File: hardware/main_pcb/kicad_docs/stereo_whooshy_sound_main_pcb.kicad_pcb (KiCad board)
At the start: 2 copper layers, 134.6 x 58.4 mm, 33 parts, among them J1 signal_in_A, J10 audio_in_B, J11 audio_out_A, J12 audio_out_B, J13 9vdc_in, J14 CV_in_B, J15 CV_in_A, J2 freq_CV_in_A, J3 signal_out_A, J4 feedback_CV_and_PS_A, J5 signal_in_B, J6 freq_CV_in_B, J7 signal_out_B, J8 feedback_CV_and_PS_B, J9 audio_in_A, U1 TL072, U2 CD74HC4067SM, U3 STM32G071KxT, U4 TL072, U5 MCP6002-xSN, U6 MCP6002-xSN, U7 MCP6002-xSN

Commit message: progress on schemo
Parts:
- removed the J11 at (81.3, 2.54)
- removed the J12 at (19.1, 2.54)
- removed the U4 at (180.0, 43.5)
- added U2: TL072, Package_SO:SOIC-8_3.9x4.9mm_P1.27mm, B.Cu at (143.5, 26.7)
- added U8: TLV1117-33, Package_TO_SOT_SMD:SOT-223-3_TabPin2, B.Cu at (158.8, 45.7)
- J10: value audio_in_B -> IO_B; footprint Connector_PinHeader_2.54mm:PinHeader_1x02_P2.54mm_Vertical -> Connector_PinHeader_2.54mm:PinHeader_1x03_P2.54mm_Vertical
- J9: value audio_in_A -> IO_A; footprint Connector_PinHeader_2.54mm:PinHeader_1x02_P2.54mm_Vertical -> Connector_PinHeader_2.54mm:PinHeader_1x03_P2.54mm_Vertical
- U1: moved to B.Cu
- U3: renamed from U5; moved to B.Cu
- U4: renamed from U6; moved to B.Cu
- U5: renamed from U7; moved to B.Cu
- U6: renamed from U2; moved to B.Cu
- U7: renamed from U3; moved to B.Cu
- moved J12 63.2 mm to (21.6, 2.54)
- moved J11 55.1 mm to (77.5, 2.54)
- moved U5 42.8 mm to (140.0, 37.9), turned to 180 degrees
- moved U3 36.3 mm to (176.5, 30.5), turned to 180 degrees
- moved U7 33.6 mm to (175.0, 17.4), turned to 180 degrees
- moved U6 25.0 mm to (150.1, 16.7), turned to 180 degrees
- moved U4 22.1 mm to (168.0, 30.5), turned to 180 degrees
- moved U1 18.3 mm to (154.9, 30.5), turned to 180 degrees
- moved J9 5.08 mm to (102.9, 2.54)
- moved J10 1.27 mm to (47.0, 2.54)
- renumbered J15 to J11, J14 to J12
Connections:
- net Net-(J10-Pad1) renamed /audio_in_B
- net Net-(J9-Pad1) renamed /audio_in_A
- J10 pad 2: GND -> /audio_out_B
- J9 pad 2: GND -> /audio_out_A
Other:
- board size 134.6 x 58.4 mm -> 134.6 x 82.6 mm

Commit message: progress on pcb layout
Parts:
- added C1: 4n7, Capacitor_SMD:C_0805_2012Metric, B.Cu at (128.9, 29.1)
- added C10: 100n, Capacitor_SMD:C_0603_1608Metric, B.Cu at (90.6, 97.8)
- added C11: 10u, Capacitor_SMD:C_0805_2012Metric, B.Cu at (45.1, 17.7)
- added C12: 100n, Capacitor_SMD:C_0603_1608Metric, B.Cu at (93.6, 97.8)
- added C13: 10u, Capacitor_SMD:C_0805_2012Metric, B.Cu at (45.1, 23.0)
- added C14: 1u, Capacitor_SMD:C_0805_2012Metric, B.Cu at (74.8, 100.0)
- added C15: 100n, Capacitor_SMD:C_0603_1608Metric, B.Cu at (78.5, 100.3)
- added C16: 4u7, Capacitor_SMD:C_0805_2012Metric, B.Cu at (51.4, 111.4)
- added C17: 100n, Capacitor_SMD:C_0603_1608Metric, B.Cu at (56.4, 111.5)
- added C18: 100n, Capacitor_SMD:C_0603_1608Metric, B.Cu at (14.7, 69.2)
- added C19: 1u, Capacitor_SMD:C_0805_2012Metric, B.Cu at (47.2, 100.4)
- added C2: 4n7, Capacitor_SMD:C_0805_2012Metric, B.Cu at (91.4, 29.3)
- added C20: 100n, Capacitor_SMD:C_0603_1608Metric, B.Cu at (14.8, 72.4)
- added C21: 1u, Capacitor_SMD:C_0805_2012Metric, B.Cu at (51.1, 100.4)
- added C22: 4u7, Capacitor_SMD:C_0805_2012Metric, B.Cu at (61.2, 90.7)
- added C23: 100n, Capacitor_SMD:C_0603_1608Metric, B.Cu at (90.8, 59.5)
- added C24: 4u7, Capacitor_SMD:C_0805_2012Metric, B.Cu at (61.2, 94.8)
- added C25: 10u bp, Capacitor_THT:C_Radial_D6.3mm_H11.0mm_P2.50mm, B.Cu at (116.2, 29.2)
- added C26: 10u bp, Capacitor_THT:C_Radial_D6.3mm_H11.0mm_P2.50mm, B.Cu at (78.7, 29.2)
- added C28: 22n, Capacitor_SMD:C_0603_1608Metric, B.Cu at (84.5, 54.8)
- added C3: 10u, Capacitor_SMD:C_0805_2012Metric, B.Cu at (95.4, 106.4)
- added C31: 100n, Capacitor_SMD:C_0603_1608Metric, B.Cu at (58.9, 59.1)
- added C33: 22n, Capacitor_SMD:C_0603_1608Metric, B.Cu at (49.5, 54.0)
- added C34: 22n, Capacitor_SMD:C_0603_1608Metric, B.Cu at (49.5, 68.2)
- added C35: 100n, Capacitor_SMD:C_0603_1608Metric, B.Cu at (82.0, 92.7)
- added C36: 100n, Capacitor_SMD:C_0603_1608Metric, B.Cu at (85.3, 92.7)
- added C37: 100n, Capacitor_SMD:C_0603_1608Metric, B.Cu at (88.6, 92.7)
- added C38: 100n, Capacitor_SMD:C_0603_1608Metric, B.Cu at (91.7, 92.7)
- added C39: 100n, Capacitor_SMD:C_0603_1608Metric, B.Cu at (94.7, 92.7)
- added C4: 100n, Capacitor_SMD:C_0603_1608Metric, B.Cu at (106.8, 28.4)
- added C40: 100n, Capacitor_SMD:C_0603_1608Metric, B.Cu at (86.5, 108.7)
- added C41: 100n, Capacitor_SMD:C_0603_1608Metric, B.Cu at (78.7, 92.7)
- added C42: 1u, Capacitor_SMD:C_0805_2012Metric, B.Cu at (79.6, 108.9)
- added C43: 1u, Capacitor_SMD:C_0805_2012Metric, B.Cu at (83.2, 108.9)
- added C44: 470n, Capacitor_SMD:C_0805_2012Metric, B.Cu at (34.2, 54.9)
- added C45: 470n, Capacitor_SMD:C_0805_2012Metric, B.Cu at (34.2, 80.7)
- added C46: 100n, Capacitor_SMD:C_0603_1608Metric, B.Cu at (48.9, 62.4)
- added C47: 100n, Capacitor_SMD:C_0603_1608Metric, B.Cu at (92.8, 66.1)
- added C48: 100n, Capacitor_SMD:C_0603_1608Metric, B.Cu at (113.2, 70.9)
- added C49: 100n, Capacitor_SMD:C_0603_1608Metric, B.Cu at (113.2, 74.9)
- added C5: 100n, Capacitor_SMD:C_0603_1608Metric, B.Cu at (106.8, 32.5)
- added C50: 100n, Capacitor_SMD:C_0603_1608Metric, B.Cu at (103.8, 70.9)
- added C51: 100n, Capacitor_SMD:C_0603_1608Metric, B.Cu at (103.8, 74.9)
- added C52: 100n, Capacitor_SMD:C_0603_1608Metric, B.Cu at (90.4, 38.8)
- added C53: 100n, Capacitor_SMD:C_0603_1608Metric, B.Cu at (90.4, 42.9)
- added C54: 100n, Capacitor_SMD:C_0603_1608Metric, B.Cu at (115.7, 39.0)
- added C55: 100n, Capacitor_SMD:C_0603_1608Metric, B.Cu at (115.7, 43.1)
- added C6: 100n, Capacitor_SMD:C_0603_1608Metric, B.Cu at (95.4, 111.8)
- added C7: 100n, Capacitor_SMD:C_0603_1608Metric, B.Cu at (34.7, 47.9)
- added C8: 100n, Capacitor_SMD:C_0603_1608Metric, B.Cu at (35.2, 73.9)
- added C9: 10u, Capacitor_SMD:C_0805_2012Metric, B.Cu at (96.9, 97.7)
- added D1: B5819W, Diode_SMD:D_SOD-123, B.Cu at (60.3, 15.9)
- added D2: PMEG2010AEH, Diode_SMD:D_SOD-123F, B.Cu at (51.9, 96.3)
- added D3: PMEG2010AEH, Diode_SMD:D_SOD-123F, B.Cu at (59.1, 101.9)
- added D4: PMEG2010AEH, Diode_SMD:D_SOD-123F, B.Cu at (59.1, 98.3)
- added D5: PMEG2010AEH, Diode_SMD:D_SOD-123F, B.Cu at (51.9, 92.7)
- added D6: LED, LED_THT:LED_D5.0mm, F.Cu at (33.7, 104.1)
- added D7: LED, LED_THT:LED_D5.0mm, F.Cu at (107.3, 104.1)
- added FB1: 100R @ 100MHz, Inductor_SMD:L_0805_2012Metric, B.Cu at (49.6, 16.5)
- added FB2: 100R @ 100MHz, Inductor_SMD:L_0805_2012Metric, B.Cu at (71.9, 92.9)
- added FB3: 100R @ 100MHz, Inductor_SMD:L_0805_2012Metric, B.Cu at (47.0, 111.6)
- added FB4: 100R @ 100MHz, Inductor_SMD:L_0805_2012Metric, B.Cu at (19.7, 70.9)
- added J14: feedback_CV_and_PS_B, Connector_PinSocket_2.54mm:PinSocket_1x08_P2.54mm_Vertical, B.Cu at (6.99, 66.0)
- added J15: swd_header, Connector_PinHeader_2.54mm:PinHeader_1x04_P2.54mm_Vertical, B.Cu at (67.3, 110.5)
- added J16: Jack-DC, Connector_BarrelJack:BarrelJack_CUI_PJ-063AH_Horizontal, B.Cu at (52.7, 12.2)
- added J17: footswitch_A, Connector_PinHeader_2.54mm:PinHeader_1x02_P2.54mm_Vertical, B.Cu at (33.7, 108.0)
- added J18: footswitch_B, Connector_PinHeader_2.54mm:PinHeader_1x02_P2.54mm_Vertical, B.Cu at (107.3, 108.0)
- added L1: 10uH, 1.2A, Inductor_SMD:L_Taiyo-Yuden_NR-50xx, B.Cu at (50.0, 105.7)
- added R1: 2M2, Resistor_SMD:R_0603_1608Metric, B.Cu at (132.7, 29.0)
- added R10: 13k3, Resistor_SMD:R_0603_1608Metric, B.Cu at (63.8, 105.9)
- added R11: 20k, Resistor_SMD:R_0603_1608Metric, B.Cu at (87.6, 59.5)
- added R12: 1k2, Resistor_SMD:R_0603_1608Metric, B.Cu at (111.1, 33.2)
- added R13: 1k2, Resistor_SMD:R_0603_1608Metric, B.Cu at (87.0, 33.6)
- added R14: 10k, Resistor_SMD:R_0603_1608Metric, B.Cu at (120.9, 29.1)
- added R15: 10k, Resistor_SMD:R_0603_1608Metric, B.Cu at (73.0, 27.8)
- added R16: R, Resistor_SMD:R_0603_1608Metric, B.Cu at (39.2, 101.9)
- added R17: R, Resistor_SMD:R_0603_1608Metric, B.Cu at (104.6, 102.3)
- added R18: 1M, Resistor_SMD:R_0603_1608Metric, B.Cu at (89.5, 72.8)
- added R19: 1M, Resistor_SMD:R_0603_1608Metric, B.Cu at (86.4, 72.8)
- added R2: 2M2, Resistor_SMD:R_0603_1608Metric, B.Cu at (125.1, 29.0)
- added R20: 300k, Resistor_SMD:R_0603_1608Metric, B.Cu at (90.8, 54.8)
- added R21: 120k, Resistor_SMD:R_0603_1608Metric, B.Cu at (87.6, 54.8)
- added R22: 10k, Resistor_SMD:R_0603_1608Metric, B.Cu at (26.8, 37.1)
- added R23: 10k, Resistor_SMD:R_0603_1608Metric, B.Cu at (15.4, 37.7)
- added R24: 100k, Resistor_SMD:R_0603_1608Metric, B.Cu at (58.9, 68.3)
- added R25: 300k, Resistor_SMD:R_0603_1608Metric, B.Cu at (62.0, 63.8)
- added R26: 120k, Resistor_SMD:R_0603_1608Metric, B.Cu at (62.0, 59.0)
- added R27: 12k, Resistor_SMD:R_0603_1608Metric, B.Cu at (62.0, 68.3)
- added R28: 10k, Resistor_SMD:R_0603_1608Metric, B.Cu at (62.2, 53.9)
- added R29: 300k, Resistor_SMD:R_0603_1608Metric, B.Cu at (49.5, 49.5)
- added R3: 2M2, Resistor_SMD:R_0603_1608Metric, B.Cu at (95.9, 29.4)
- added R30: 120k, Resistor_SMD:R_0603_1608Metric, B.Cu at (52.6, 49.5)
- added R31: 120k, Resistor_SMD:R_0603_1608Metric, B.Cu at (55.9, 49.6)
- added R32: 120k, Resistor_SMD:R_0603_1608Metric, B.Cu at (58.9, 49.5)
- added R33: 300k, Resistor_SMD:R_0603_1608Metric, B.Cu at (55.9, 53.9)
- added R34: 100k, Resistor_SMD:R_0603_1608Metric, B.Cu at (58.9, 53.9)
- added R35: 300k, Resistor_SMD:R_0603_1608Metric, B.Cu at (49.5, 72.7)
- added R36: 300k, Resistor_SMD:R_0603_1608Metric, B.Cu at (52.6, 72.7)
- added R37: 120k, Resistor_SMD:R_0603_1608Metric, B.Cu at (58.9, 72.7)
- added R38: 120k, Resistor_SMD:R_0603_1608Metric, B.Cu at (62.0, 72.7)
- added R4: 2M2, Resistor_SMD:R_0603_1608Metric, B.Cu at (87.0, 29.5)
- added R40: 120k, Resistor_SMD:R_0603_1608Metric, B.Cu at (52.6, 53.9)
- added R41: 120k, Resistor_SMD:R_0603_1608Metric, B.Cu at (52.6, 68.3)
- added R42: 10k, Resistor_SMD:R_0603_1608Metric, B.Cu at (75.4, 92.6)
- added R43: 20k, Resistor_SMD:R_0603_1608Metric, B.Cu at (26.8, 40.9)
- added R44: 10k, Resistor_SMD:R_0603_1608Metric, B.Cu at (29.8, 40.9)
- added R45: 30k, Resistor_SMD:R_0603_1608Metric, B.Cu at (23.7, 40.8)
- added R46: 4k7, Resistor_SMD:R_0603_1608Metric, B.Cu at (35.9, 40.9)
- added R47: 1k2, Resistor_SMD:R_0603_1608Metric, B.Cu at (32.9, 40.9)
- added R48: 100k, Resistor_SMD:R_0603_1608Metric, B.Cu at (27.8, 54.9)
- added R49: 100k, Resistor_SMD:R_0603_1608Metric, B.Cu at (30.9, 54.9)
- added R5: 2k2, Resistor_SMD:R_0603_1608Metric, B.Cu at (19.7, 75.7)
- added R50: 100k, Resistor_SMD:R_0603_1608Metric, B.Cu at (24.8, 54.9)
- added R51: 10k, Resistor_SMD:R_0603_1608Metric, B.Cu at (42.8, 101.9)
- added R52: 10k, Resistor_SMD:R_0603_1608Metric, B.Cu at (101.2, 102.3)
- added R53: 1M, Resistor_SMD:R_0603_1608Metric, B.Cu at (42.8, 105.6)
- added R54: 1M, Resistor_SMD:R_0603_1608Metric, B.Cu at (101.2, 106.2)
- added R55: 300k, Resistor_SMD:R_0603_1608Metric, B.Cu at (58.9, 63.8)
- added R57: 20k, Resistor_SMD:R_0603_1608Metric, B.Cu at (29.8, 67.1)
- added R58: 10k, Resistor_SMD:R_0603_1608Metric, B.Cu at (26.8, 67.1)
- added R59: 30k, Resistor_SMD:R_0603_1608Metric, B.Cu at (23.7, 67.1)
- added R6: 1R, Resistor_SMD:R_0603_1608Metric, B.Cu at (47.2, 95.6)
- added R60: 4k7, Resistor_SMD:R_0603_1608Metric, B.Cu at (35.9, 67.1)
- added R61: 1k2, Resistor_SMD:R_0603_1608Metric, B.Cu at (32.9, 67.1)
- added R62: 100k, Resistor_SMD:R_0603_1608Metric, B.Cu at (27.8, 80.6)
- added R63: 100k, Resistor_SMD:R_0603_1608Metric, B.Cu at (30.9, 80.6)
- added R64: 100k, Resistor_SMD:R_0603_1608Metric, B.Cu at (24.8, 80.6)
- added R65: 300k, Resistor_SMD:R_0603_1608Metric, B.Cu at (55.9, 72.7)
- added R66: 300k, Resistor_SMD:R_0603_1608Metric, B.Cu at (55.9, 68.3)
- added R7: 1R, Resistor_SMD:R_0603_1608Metric, B.Cu at (54.4, 100.5)
- added R8: 100k, Resistor_SMD:R_0603_1608Metric, B.Cu at (84.5, 59.5)
- added R9: 114k, Resistor_SMD:R_0603_1608Metric, B.Cu at (60.7, 105.9)
- added RV12: 100k trim, custom_footprints:bourns_3306F, B.Cu at (22.2, 30.5)
- added RV13: 100k trim, custom_footprints:bourns_3306F, B.Cu at (6.99, 30.5)
- added RV14: 100k trim, custom_footprints:bourns_3306F, B.Cu at (52.8, 30.5)
- added RV15: 100k trim, custom_footprints:bourns_3306F, B.Cu at (37.5, 30.5)
- added SW1: SW_DP_on_on_on, custom_footprints:DPDT_mini_toggle, F.Cu at (71.8, 36.8)
- added SW2: SW_SPDT_center_off, custom_footprints:SPDT_mini_toggle, F.Cu at (71.8, 58.4)
- added SW3: SW_SPDT, custom_footprints:SPDT_mini_toggle, F.Cu at (71.8, 80.0)
- added SW4: SW_DPDT_center_off, custom_footprints:DPDT_mini_toggle, F.Cu at (43.8, 80.0)
- added U10: STM32L031F4Px, Package_SO:TSSOP-20_4.4x6.5mm_P0.65mm, B.Cu at (84.6, 100.1)
- added U11: MCP4822, Package_SO:TSSOP-8_3x3mm_P0.65mm, B.Cu at (91.2, 108.7)
- added U12: LT1117-3.3, Package_TO_SOT_SMD:SOT-223-3_TabPin2, B.Cu at (52.2, 21.3)
- added U13: LT3467A, Package_TO_SOT_SMD:TSOT-23-6, B.Cu at (56.4, 107.2)
- added U14: LM4040DBZ-5, Package_TO_SOT_SMD:SOT-23, B.Cu at (14.9, 76.1)
- added U9: DG469EQ, Package_SO:MSOP-8_3x3mm_P0.65mm, B.Cu at (110.9, 40.9)
- J1: value signal_in_A -> NRJ6HM-1; footprint Connector_PinSocket_2.54mm:PinSocket_1x04_P2.54mm_Vertical -> Connector_Audio:Jack_6.35mm_Neutrik_NRJ6HM-1_Horizontal
- J10: value IO_B -> feedback_CV_and_PS_A; footprint Connector_PinHeader_2.54mm:PinHeader_1x03_P2.54mm_Vertical -> Connector_PinSocket_2.54mm:PinSocket_1x08_P2.54mm_Vertical
- J11: value CV_in_A -> signal_in_B; footprint Connector_PinHeader_2.54mm:PinHeader_1x03_P2.54mm_Vertical -> Connector_PinSocket_2.54mm:PinSocket_1x04_P2.54mm_Vertical
- J12: value CV_in_B -> signal_out_B; footprint Connector_PinHeader_2.54mm:PinHeader_1x03_P2.54mm_Vertical -> Connector_PinSocket_2.54mm:PinSocket_1x04_P2.54mm_Vertical
- J13: value 9vdc_in -> freq_CV_in_B; footprint Connector_PinHeader_2.54mm:PinHeader_1x02_P2.54mm_Vertical -> Connector_PinSocket_2.54mm:PinSocket_1x04_P2.54mm_Vertical
- J2: value freq_CV_in_A -> NRJ6HM-1; footprint Connector_PinSocket_2.54mm:PinSocket_1x04_P2.54mm_Vertical -> Connector_Audio:Jack_6.35mm_Neutrik_NRJ6HM-1_Horizontal
- J3: value signal_out_A -> NRJ6HM-1; footprint Connector_PinSocket_2.54mm:PinSocket_1x04_P2.54mm_Vertical -> Connector_Audio:Jack_6.35mm_Neutrik_NRJ6HM-1_Horizontal
- J4: value feedback_CV_and_PS_A -> NRJ6HM-1; footprint Connector_PinSocket_2.54mm:PinSocket_1x08_P2.54mm_Vertical -> Connector_Audio:Jack_6.35mm_Neutrik_NRJ6HM-1_Horizontal
- J5: value signal_in_B -> NRJ6HM-1; footprint Connector_PinSocket_2.54mm:PinSocket_1x04_P2.54mm_Vertical -> Connector_Audio:Jack_6.35mm_Neutrik_NRJ6HM-1_Horizontal
- J6: value freq_CV_in_B -> NRJ6HM-1; footprint Connector_PinSocket_2.54mm:PinSocket_1x04_P2.54mm_Vertical -> Connector_Audio:Jack_6.35mm_Neutrik_NRJ6HM-1_Horizontal
- J7: value signal_out_B -> signal_in_A
- J8: value feedback_CV_and_PS_B -> signal_out_A; footprint Connector_PinSocket_2.54mm:PinSocket_1x08_P2.54mm_Vertical -> Connector_PinSocket_2.54mm:PinSocket_1x04_P2.54mm_Vertical
- J9: value IO_A -> freq_CV_in_A; footprint Connector_PinHeader_2.54mm:PinHeader_1x03_P2.54mm_Vertical -> Connector_PinSocket_2.54mm:PinSocket_1x04_P2.54mm_Vertical
- RV4: value 10k -> 500k_dual; footprint Potentiometer_THT:Potentiometer_Alpha_RD901F-40-00D_Single_Vertical -> Potentiometer_THT:Potentiometer_Alpha_RD902F-40-00D_Dual_Vertical
- RV5: value 10k -> 10k_dual; footprint Potentiometer_THT:Potentiometer_Alpha_RD901F-40-00D_Single_Vertical -> Potentiometer_THT:Potentiometer_Alpha_RD902F-40-00D_Dual_Vertical
- U1: value TL072 -> TL074; footprint Package_SO:SOIC-8_3.9x4.9mm_P1.27mm -> Package_SO:TSSOP-14_4.4x5mm_P0.65mm
- U2: value TL072 -> MCP6004; footprint Package_SO:SOIC-8_3.9x4.9mm_P1.27mm -> Package_SO:TSSOP-14_4.4x5mm_P0.65mm
- U3, U4, U5: value MCP6002-xSN -> MCP6004; footprint Package_SO:SOIC-8_3.9x4.9mm_P1.27mm -> Package_SO:TSSOP-14_4.4x5mm_P0.65mm
- U6: value CD74HC4067SM -> DG469EQ; footprint Package_SO:SSOP-24_5.3x8.2mm_P0.65mm -> Package_SO:MSOP-8_3x3mm_P0.65mm
- U7: value STM32G071KxT -> DG469EQ; footprint Package_QFP:LQFP-32_7x7mm_P0.8mm -> Package_SO:MSOP-8_3x3mm_P0.65mm
- U8: value TLV1117-33 -> DG469EQ; footprint Package_TO_SOT_SMD:SOT-223-3_TabPin2 -> Package_SO:MSOP-8_3x3mm_P0.65mm
- moved U3 152.9 mm to (29.8, 73.9), turned to 270 degrees
- moved J7 136.5 mm to (134.0, 38.1)
- moved RV11 119.2 mm to (122.6, 87.6)
- moved U4 118.1 mm to (54.0, 61.1), turned to 270 degrees
- moved U2 116.0 mm to (29.5, 47.9), turned to 270 degrees
- moved J13 103.4 mm to (60.3, 76.2)
- moved U7 94.0 mm to (99.2, 72.9), turned to 270 degrees
- moved RV5 92.5 mm to (41.3, 66.1)
- moved RV3 90.2 mm to (13.4, 87.6)
- moved RV6 88.8 mm to (95.9, 44.5)
- moved J9 80.0 mm to (134.0, 76.2), turned to 180 degrees
- moved J8 79.5 mm to (80.6, 38.1)
- moved U8 72.9 mm to (86.0, 40.9), turned to 270 degrees
- moved J10 71.9 mm to (80.6, 66.0), turned to 180 degrees
- moved U6 70.0 mm to (108.3, 72.9), turned to 270 degrees
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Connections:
- J10 pad 1: /audio_in_B -> GND
- J10 pad 2: /audio_out_B -> GND
- J10 pad 3: Net-(J10-Pad3) -> /VCF_plug_in_board_ports/feedback_CV_in_A
- J11 pad 1: Net-(J11-Pad1) -> GND
- J11 pad 2: Net-(J11-Pad2) -> GND
- J11 pad 3: Net-(J11-Pad3) -> /switched_dry_B
- J12 pad 1: Net-(J12-Pad1) -> GND
- J12 pad 2: Net-(J12-Pad2) -> GND
- J12 pad 3: Net-(J12-Pad3) -> /bypass_switches/wet_in_B
- J13 pad 1: Net-(J13-Pad1) -> GND
- J13 pad 2: Net-(J13-Pad2) -> GND
- J7 pad 1: Net-(J7-Pad1) -> GND
- J7 pad 2: Net-(J7-Pad2) -> GND
- J7 pad 3: Net-(J7-Pad3) -> /dry_A
- J7 pad 4: Net-(J7-Pad4) -> /dry_A
- J8 pad 1: Net-(J8-Pad1) -> GND
- J8 pad 2: Net-(J8-Pad2) -> GND
- J8 pad 3: Net-(J8-Pad3) -> /wet_A
- J8 pad 4: Net-(J8-Pad4) -> /wet_A
- J9 pad 1: /audio_in_A -> GND
- J9 pad 2: /audio_out_A -> GND
- J9 pad 3: Net-(J9-Pad3) -> /VCF_plug_in_board_ports/freq_CV_in_A
- RV1 pad 2: /control_voltage_generators/scanned_potentiometers/initial_freq -> /control_voltage_generators/cv_summers/manual_freq
- RV1 pad 3: +3.3VA -> -5V
- RV10 pad 2: /control_voltage_generators/scanned_potentiometers/depth_B -> /control_voltage_generators/lfo/lfo_2_shape_cv
- RV11 pad 2: /control_voltage_generators/scanned_potentiometers/feedback -> /control_voltage_generators/lfo/lfo_2_depth_cv
- RV2 pad 2: /control_voltage_generators/scanned_potentiometers/env_lev_A -> /control_voltage_generators/cv_summers/separation_B
- RV2 pad 3: +3.3VA -> -5V
- RV3 pad 2: /control_voltage_generators/scanned_potentiometers/rate_A -> Net-(R20-Pad2)
- RV3 pad 3: +3.3VA -> -5V
- RV4 pad 1: GND -> Net-(R46-Pad1)
- RV4 pad 2: /control_voltage_generators/scanned_potentiometers/shape_A -> Net-(C44-Pad1)
- RV4 pad 3: +3.3VA -> Net-(C44-Pad1)
- RV5 pad 1: GND -> +1V0
- RV5 pad 2: /control_voltage_generators/scanned_potentiometers/depth_A -> /control_voltage_generators/cv_summers/env_A
- RV5 pad 3: +3.3VA -> Net-(R50-Pad1)
- RV6 pad 2: /control_voltage_generators/scanned_potentiometers/separation -> /control_voltage_generators/lfo/lfo_1_rate_cv
- RV7 pad 2: /control_voltage_generators/scanned_potentiometers/env_lev_B -> /control_voltage_generators/lfo/lfo_1_shape_cv
- RV8 pad 2: /control_voltage_generators/scanned_potentiometers/rate_B -> /control_voltage_generators/lfo/lfo_1_depth_cv
- RV9 pad 2: /control_voltage_generators/scanned_potentiometers/shape_B -> /control_voltage_generators/lfo/lfo_2_rate_cv
- U1 pad 1: Net-(U1-Pad1) -> Net-(R12-Pad2)
- U1 pad 2: Net-(U1-Pad2) -> Net-(R12-Pad2)
- U1 pad 3: Net-(U1-Pad3) -> /audio_output_buffers/audio_in_A
- U1 pad 4: (no net) -> +12V
- U1 pad 6: Net-(U1-Pad6) -> /dry_A
- U1 pad 7: Net-(U1-Pad7) -> /dry_A
- U1 pad 8: (no net) -> Net-(R13-Pad2)
- U2 pad 3: Net-(U2-Pad3) -> GND
- U2 pad 4: (no net) -> +3V3
- U2 pad 8: (no net) -> Net-(R48-Pad2)
- U3 pad 3: Net-(U3-Pad3) -> GND
- U3 pad 4: (no net) -> +3V3
- U3 pad 8: (no net) -> Net-(R62-Pad2)
- U4 pad 1: Net-(U4-Pad1) -> /VCF_plug_in_board_ports/freq_CV_in_A
- U4 pad 4: (no net) -> +3V3
- U4 pad 5: Net-(U4-Pad5) -> GND
- U4 pad 7: Net-(U4-Pad7) -> /control_voltage_generators/cv_summers/separation_A
- U4 pad 8: (no net) -> Net-(U4-Pad8)
- U5 pad 1: Net-(U5-Pad1) -> /VCF_plug_in_board_ports/feedback_CV_in_A
- U5 pad 3: Net-(U5-Pad3) -> GND
- U5 pad 4: (no net) -> +3V3
- U5 pad 5: Net-(U5-Pad5) -> GND
- U5 pad 7: Net-(U5-Pad7) -> +1V0
- U5 pad 8: (no net) -> Net-(D6-Pad2)
- U6 pad 1: Net-(U6-Pad1) -> /VCF_plug_in_board_ports/freq_CV_in_A
- U6 pad 3: Net-(U6-Pad3) -> GND
- U6 pad 4: Net-(U6-Pad4) -> +12V
- U6 pad 5: Net-(U6-Pad5) -> (no net)
- U6 pad 6: Net-(U6-Pad6) -> /bypass_switches/bypass_logic_in_A
- U6 pad 7: Net-(U6-Pad7) -> -12V
- U6 pad 8: Net-(U6-Pad8) -> Net-(R18-Pad2)
- U7 pad 1: Net-(U7-Pad1) -> /VCF_plug_in_board_ports/freq_CV_in_B
- U7 pad 3: Net-(U7-Pad3) -> GND
- U7 pad 4: Net-(U7-Pad4) -> +12V
- U7 pad 5: Net-(U7-Pad5) -> (no net)
- U7 pad 6: Net-(U7-Pad6) -> /bypass_switches/bypass_logic_in_B
- U7 pad 7: Net-(U7-Pad7) -> -12V
- U7 pad 8: Net-(U7-Pad8) -> Net-(R19-Pad2)
- U8 pad 1: Net-(U8-Pad1) -> /audio_output_buffers/audio_in_A
- U8 pad 2: Net-(U8-Pad2) -> /dry_A
- U8 pad 3: Net-(U8-Pad3) -> GND
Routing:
- net +3V3: track 0.00 -> 427.6 mm, vias 0 -> 18
- net -12V: track 0.00 -> 280.9 mm, vias 0 -> 5
- net +12V: track 0.00 -> 273.6 mm, vias 0 -> 5
- net +9V: track 0.00 -> 271.9 mm, vias 0 -> 7
- net GND: track 0.00 -> 228.1 mm, vias 0 -> 75
- net /bypass_switches/bypass_logic_in_A: track 0.00 -> 170.7 mm, vias 0 -> 4
- net +3.3VA: track 0.00 -> 166.7 mm, vias 0 -> 2
- net /dry_A: track 0.00 -> 166.4 mm, vias 0 -> 3
- net -5V: track 0.00 -> 161.1 mm, vias 0 -> 4
- net /VCF_plug_in_board_ports/freq_CV_in_A: track 0.00 -> 120.5 mm, vias 0 -> 2
- net /bypass_switches/wet_in_B: track 0.00 -> 114.7 mm, vias 0 -> 1
- net Net-(R20-Pad2): track 0.00 -> 113.4 mm, vias 0 -> 2
- net +1V0: track 0.00 -> 108.1 mm, vias 0 -> 2
- net /VCF_plug_in_board_ports/feedback_CV_in_A: track 0.00 -> 106.9 mm
- net Net-(D6-Pad1): track 0.00 -> 105.8 mm, vias 0 -> 2
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- added copper zone on GND_layer, net GND
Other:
- board size 134.6 x 82.6 mm -> 134.6 x 113 mm
- copper layers 2 -> 4
- board text added: "+12vdc"
- board text added: "+3.3v"
- board text added: "+9vdc in"
- board text added: "-12vdc"
- board text added: "9vdc in"
- board text added: "A"
- board text added: "B"
- board text added: "B input"
- board text added: "B-input"
- board text added: "CV in A"
- board text added: "CV in B"
- board text added: "LED A"
- board text added: "LED B"
- board text added: "LFO A depth"
- board text added: "LFO A rate"
- board text added: "LFO A shape"
- board text added: "LFO B depth"
- board text added: "LFO B invert"
- board text added: "LFO B rate"
- board text added: "LFO B shape"
- board text added: "LFO mode"
- board text added: "Stereo Whooshy Sound filter pedal rev 0 github.com/JordanAceto/stereo_whooshy_sound"
- board text added: "VCF plug-in board port A"
- board text added: "VCF plug-in board port B"
- board text added: "attack"
- board text added: "dry A"
- board text added: "dry B"
- board text added: "env. attack"
- board text added: "env. level"
- board text added: "env. mode"
- board text added: "envelope"
- board text added: "envelope A level trim"
- board text added: "envelope B level trim"
- board text added: "exp pedal A trim"
- board text added: "exp pedal B trim"
- board text added: "exp. current A"
- board text added: "exp. current B"
- board text added: "foot switch A"
- board text added: "foot switch B"
- board text added: "footswitch A"
- board text added: "footswitch B"
- board text added: "freq."
- board text added: "freq. CV A"
- board text added: "freq. CV B"
- board text added: "gnd"
- board text added: "in A"
- board text added: "in B"
- board text added: "level"
- board text added: "manual"
- board text added: "manual freq."
- board text added: "out A"
- board text added: "out B"
- board text added: "res."
- board text added: "res. CV A"
- board text added: "res. CV B"
- board text added: "sep."
- board text added: "stereo whooshy sound"
- board text added: "swclk"
- board text added: "swd header"
- board text added: "swdio"
- board text added: "sweep generators"
- board text added: "wet A"
- board text added: "wet B"
- board text removed: "dwn dwn"
- board text removed: "env A"
- board text removed: "env B"
- board text removed: "env mode"
- board text removed: "initial freq"
- board text removed: "up dwn"
- board text removed: "up up"

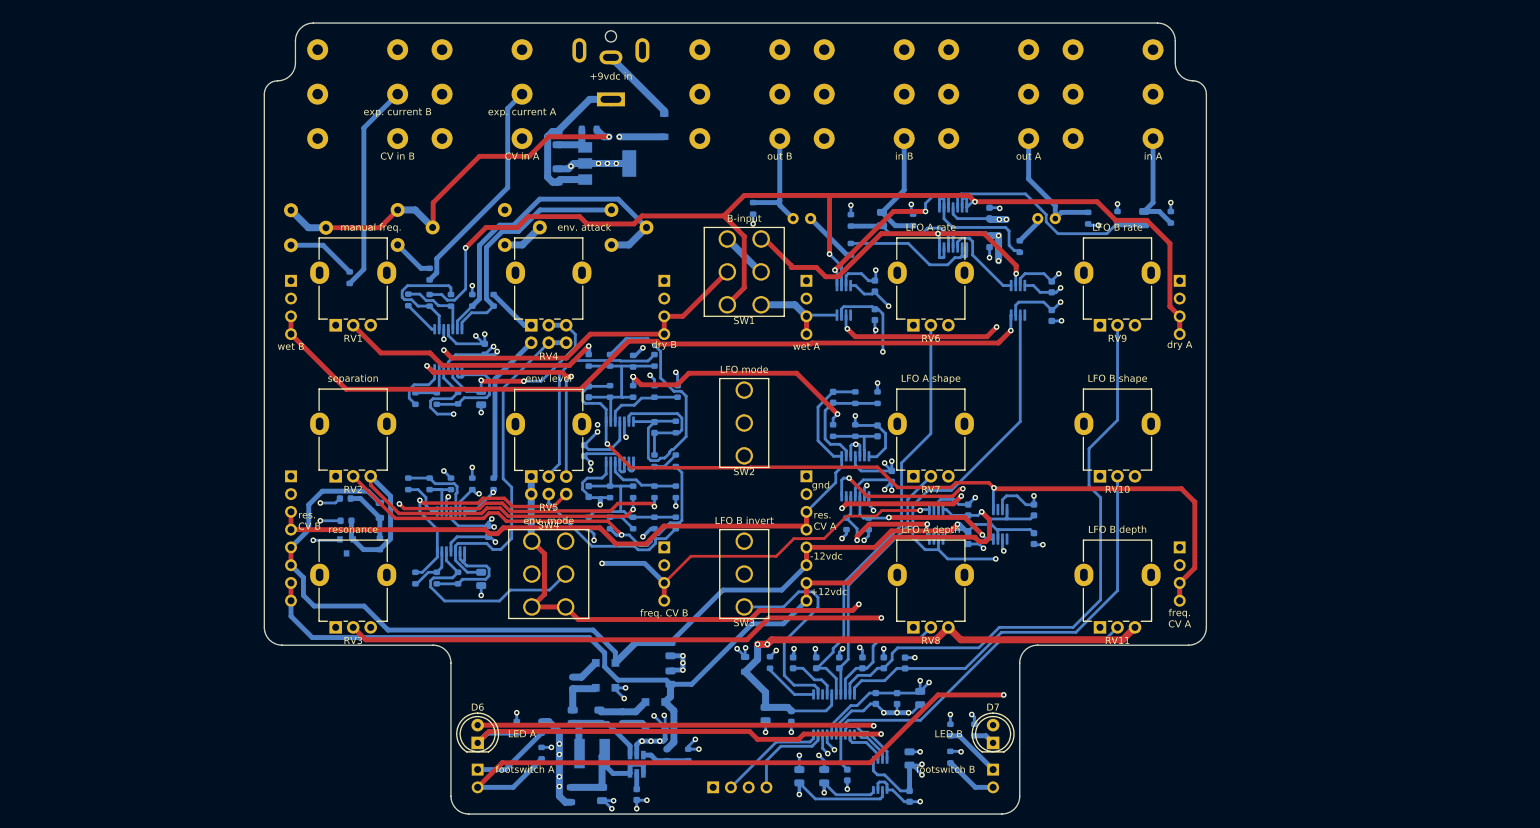
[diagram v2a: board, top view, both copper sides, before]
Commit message: reduce analog switch count, tidy up
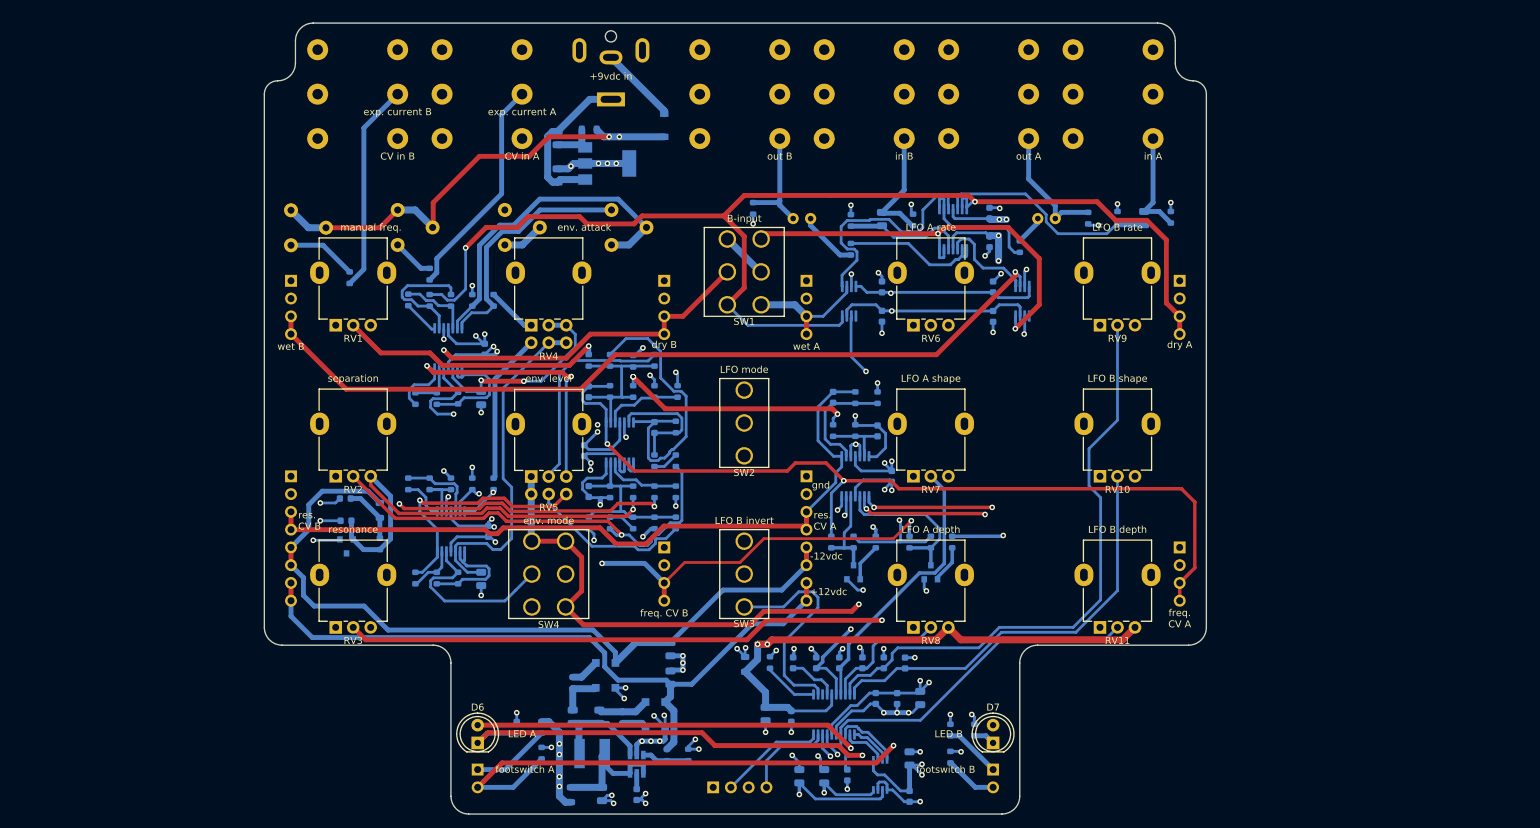
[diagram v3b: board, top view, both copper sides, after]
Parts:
- removed C52, C53, C54, C55: 100n, Capacitor_SMD:C_0603_1608Metric
- removed the U8 at (86.0, 40.9)
- removed the U9 at (110.9, 40.9)
- added Q1: MMBT3904, Package_TO_SOT_SMD:SOT-23, B.Cu at (87.4, 79.8)
- added Q2: MMBT3904, Package_TO_SOT_SMD:SOT-23, B.Cu at (98.4, 79.8)
- added R39: 120k, Resistor_SMD:R_0603_1608Metric, B.Cu at (98.4, 75.4)
- added R56: 12k, Resistor_SMD:R_0603_1608Metric, B.Cu at (95.4, 75.4)
- added R67: 120k, Resistor_SMD:R_0603_1608Metric, B.Cu at (90.6, 75.4)
- added R68: 120k, Resistor_SMD:R_0603_1608Metric, B.Cu at (101.5, 75.4)
- R16, R17: value R -> 1k2
- R18: value 1M -> 120k
- R19: value 1M -> 12k
- moved U6 38.5 mm to (86.7, 41.0)
- moved C50 34.2 mm to (91.4, 39.0)
- moved U7 34.2 mm to (111.5, 41.0)
- moved C51 34.1 mm to (91.4, 43.2)
- moved C48 32.4 mm to (107.3, 39.0)
- moved C49 32.3 mm to (107.3, 43.2)
- moved R19 3.38 mm to (84.2, 75.4)
- moved R18 3.38 mm to (87.4, 75.4)
- moved U1 0.25 mm to (101.6, 30.7)
- moved U2 0.13 mm to (29.5, 47.8)
- moved U4 0.13 mm to (54.0, 61.2)
- turned SW4 to 0 degrees
- renumbered U12 to U10, U13 to U11, U14 to U12, U10 to U8, U11 to U9
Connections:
- R18 pad 1: GND -> Net-(Q1-Pad3)
- R18 pad 2: Net-(R18-Pad2) -> +3V3
- R19 pad 1: GND -> Net-(Q1-Pad3)
- R19 pad 2: Net-(R19-Pad2) -> /VCF_plug_in_board_ports/freq_CV_in_A
- U5 pad 10: Net-(R18-Pad2) -> Net-(Q2-Pad3)
- U5 pad 12: Net-(R19-Pad2) -> Net-(Q1-Pad3)
- U5 pad 13: Net-(D7-Pad1) -> Net-(D6-Pad1)
- U5 pad 14: Net-(D7-Pad2) -> Net-(D6-Pad2)
- U5 pad 8: Net-(D6-Pad2) -> Net-(D7-Pad2)
- U5 pad 9: Net-(D6-Pad1) -> Net-(D7-Pad1)
- U6 pad 1: /VCF_plug_in_board_ports/freq_CV_in_A -> /audio_output_buffers/audio_in_A
- U6 pad 2: Net-(U6-Pad2) -> /wet_A
- U6 pad 8: Net-(R18-Pad2) -> /dry_A
- U7 pad 1: /VCF_plug_in_board_ports/freq_CV_in_B -> /audio_output_buffers/audio_in_B
- U7 pad 2: Net-(U7-Pad2) -> /bypass_switches/wet_in_B
- U7 pad 8: Net-(R19-Pad2) -> /dry_B
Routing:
- net -12V: track 280.9 -> 230.1 mm, vias 5 -> 3
- net +12V: track 273.6 -> 223.7 mm, vias 5 -> 3
- net /bypass_switches/bypass_logic_in_A: track 170.7 -> 139.3 mm, vias 4 -> 3
- net GND: track 228.1 -> 202.2 mm, vias 75 -> 73
- net Net-(Q2-Pad3): track 0.00 -> 23.3 mm
- net Net-(R18-Pad2): track 23.2 -> 0.00 mm, vias 2 -> 0
- net Net-(R19-Pad2): track 20.7 -> 0.00 mm, vias 2 -> 0
- net +3V3: track 427.6 -> 442.8 mm, vias 18 -> 19
- net Net-(Q1-Pad3): track 0.00 -> 13.4 mm
- net /bypass_switches/bypass_logic_in_B: track 96.6 -> 84.1 mm, vias 1 -> 2
- net /dry_B: track 52.0 -> 61.4 mm
- net /audio_output_buffers/audio_in_A: track 25.3 -> 33.0 mm, vias 2 -> 0
- net Net-(D7-Pad2): track 57.2 -> 49.9 mm
- net /VCF_plug_in_board_ports/freq_CV_in_A: track 120.5 -> 126.4 mm
- net Net-(Q1-Pad1): track 0.00 -> 5.41 mm
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
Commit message: tidy up kicad docs
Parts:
- renumbered C48 to C27, C49 to C29, C50 to C30, C51 to C32
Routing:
- net GND: track 202.2 -> 207.5 mm
- net Net-(R60-Pad2): track 50.1 -> 51.3 mm
- net /control_voltage_generators/cv_summers/separation_B: track 65.7 -> 65.0 mm
- net Net-(R61-Pad2): track 48.8 -> 49.4 mm
